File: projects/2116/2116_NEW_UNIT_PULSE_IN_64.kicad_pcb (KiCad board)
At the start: 2 copper layers, 166 x 180 mm, 172 parts, among them CN1 09031966921, CN10 HIF3FC-16PA-2.54DSA, CN11 HIF3FC-16PA-2.54DSA, CN2 09232486824, CN3 B2B-XH-A, CN4 HIF3FC-16PA-2.54DS, CN5 HIF3FC-16PA-2.54DS, CN6 HIF3FC-16PA-2.54DSA, CN7 HIF3FC-16PA-2.54DSA, CN8 HIF3FC-16PA-2.54DS, CN9 HIF3FC-16PA-2.54DS, IC1 74HCT32, IC10 74HC244, IC11 74HC244, IC12 74HC244, IC13 74HC14, IC14 74HC14, IC15 74HC14, IC16 74HC14, IC17 74HC14, IC18 74HC14, IC19 74HC244, IC2 74HCT138, IC20 74HC244, IC21 74HC244, IC22 74HC244, IC23 74HCT32, IC24 74HCT574, IC25 74HCT574, IC26 74HCT574, IC27 74HCT574, IC28 74HCT541, IC29 74HCT541, IC3 74HC14, IC30 74HCT541, IC31 74HCT541, IC32 74HCT574, IC33 74HCT574, IC34 74HCT574, IC35 74HCT574, IC36 74HCT541, IC37 74HCT541, IC38 74HCT541, IC39 74HCT541, IC4 74HC14, IC5 74HC14, IC6 74HC14, IC7 74HC14, IC8 74HC14, IC9 74HC244

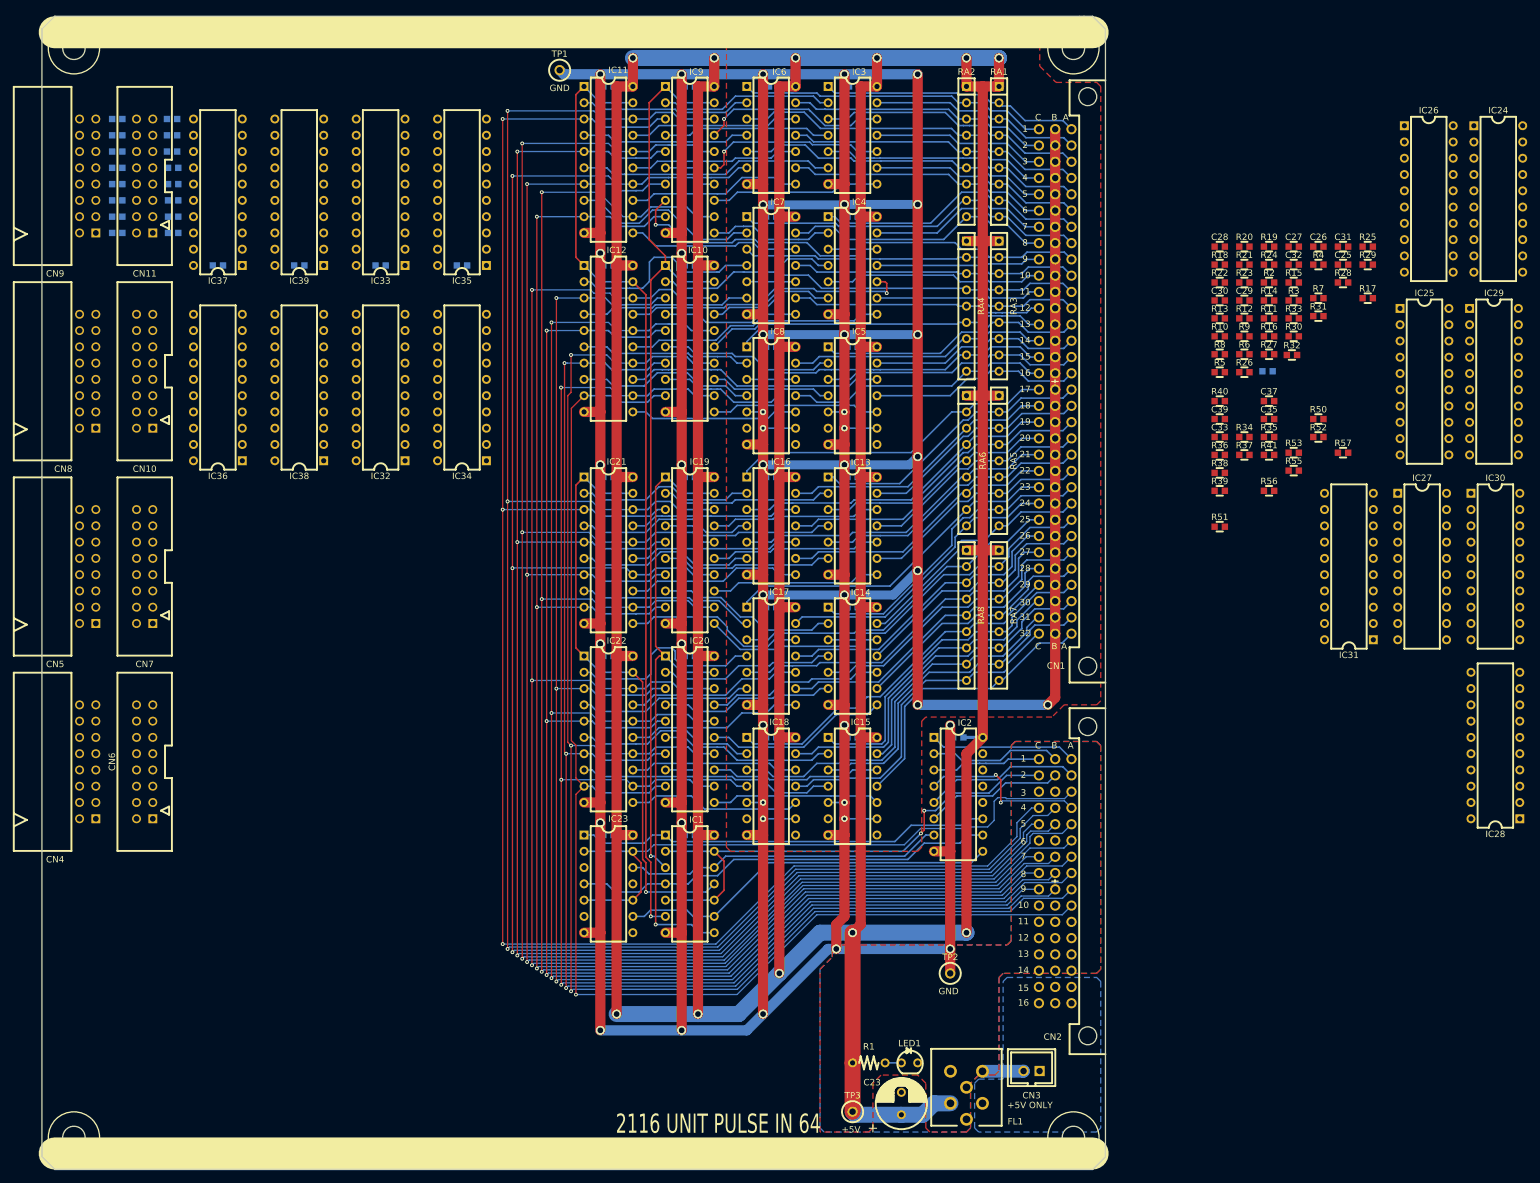
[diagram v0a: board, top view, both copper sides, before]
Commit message: 基板端に電源コネクタを追加。
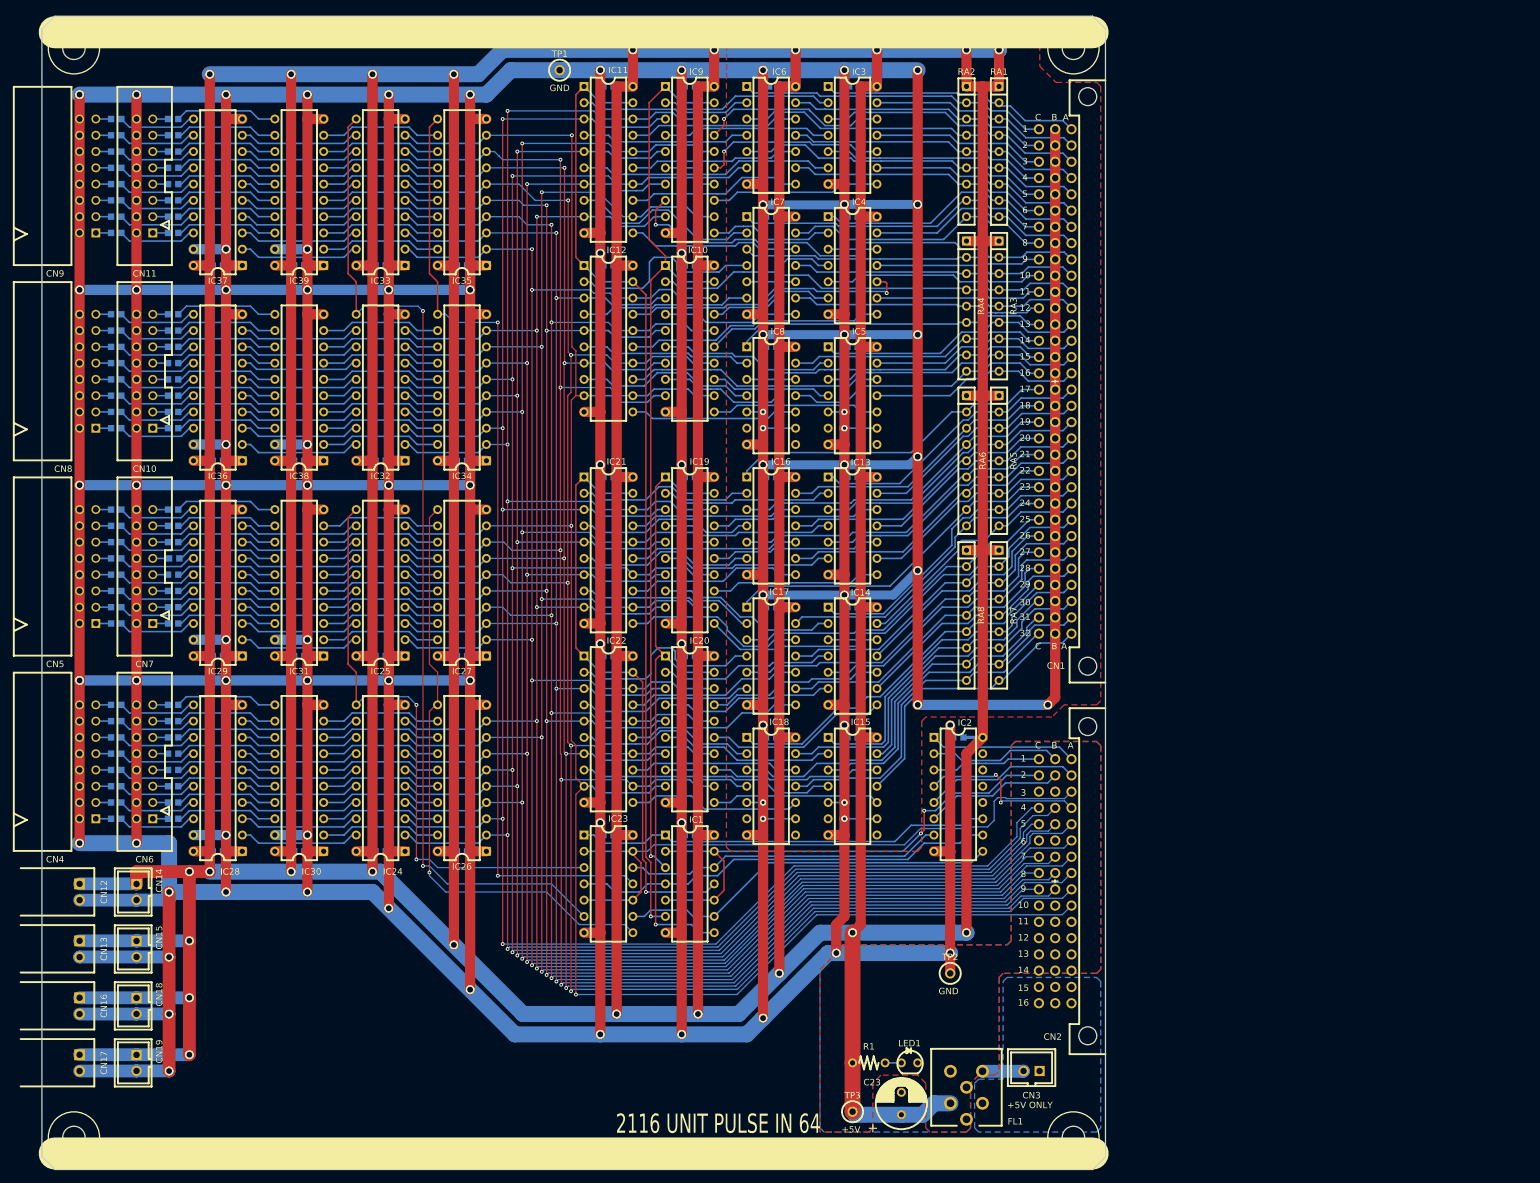
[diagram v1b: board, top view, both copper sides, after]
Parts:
- added CN12: S2B-XH-A, A01myFootPrint:S2B-XH-A, F.Cu at (55.9, 185.4)
- added CN13: S2B-XH-A, A01myFootPrint:S2B-XH-A, F.Cu at (55.9, 194.3)
- added CN14: B2B-XH-A, A01myFootPrint:cn_B2B-XH-A, F.Cu at (64.8, 186.7)
- added CN15: B2B-XH-A, A01myFootPrint:cn_B2B-XH-A, F.Cu at (64.8, 195.6)
- added CN16: S2B-XH-A, A01myFootPrint:S2B-XH-A, F.Cu at (55.9, 203.2)
- added CN17: S2B-XH-A, A01myFootPrint:S2B-XH-A, F.Cu at (55.9, 212.1)
- added CN18: B2B-XH-A, A01myFootPrint:cn_B2B-XH-A, F.Cu at (64.8, 204.5)
- added CN19: B2B-XH-A, A01myFootPrint:cn_B2B-XH-A, F.Cu at (64.8, 213.4)
- C25, C26, C27, C28, C29, C30, C31, C32, C33, C35, C37, C39, R10, R11, R12, R13, R14, R15, R16, R17, R18, R19, R2, R20, R21, R22, R23, R24, R25, R26, R27, R28, R29, R3, R30, R31, R32, R33, R34, R35, R36, R37, R38, R39, R4, R40, R41, R5, R50, R51, R52, R53, R55, R56, R57, R6, R7, R8, R9: moved to B.Cu
- moved R4 204.5 mm to (61.6, 170.2), turned to 180 degrees
- moved IC24 201.6 mm to (106.7, 180.3), turned to 180 degrees
- moved R3 199.8 mm to (61.6, 172.7), turned to 180 degrees
- moved R7 199.8 mm to (61.6, 162.6), turned to 180 degrees
- moved R25 199.7 mm to (70.5, 157.5), turned to 180 degrees
- moved IC28 199.5 mm to (81.3, 180.3)
- moved IC29 199.1 mm to (81.3, 149.9), turned to 180 degrees
- moved R2 198.5 mm to (61.6, 175.3), turned to 180 degrees
- moved R17 198.1 mm to (61.6, 127.0), turned to 180 degrees
- moved R29 192.6 mm to (70.5, 137.2), turned to 180 degrees
- moved R19 191.8 mm to (70.5, 172.7), turned to 180 degrees
- moved R28 188.8 mm to (70.5, 139.7), turned to 180 degrees
- moved C31 188.3 mm to (90.2, 180.3)
- moved R15 188.2 mm to (61.6, 132.1), turned to 180 degrees
- moved IC30 187.6 mm to (94.0, 180.3), turned to 180 degrees
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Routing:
- net GND: track 1188.5 -> 2561.7 mm, vias 43 -> 85
- net +5V: track 1026.3 -> 1875.7 mm, vias 11 -> 23
- net /W01: track 0.00 -> 157.8 mm, vias 0 -> 2
- net /W03: track 0.00 -> 149.4 mm, vias 0 -> 2
- net /D15: track 205.8 -> 301.6 mm, vias 1 -> 3
- net /W02: track 0.00 -> 94.1 mm, vias 0 -> 1
- net /W00: track 0.00 -> 92.8 mm, vias 0 -> 2
- net /D14: track 224.4 -> 311.8 mm, vias 3 -> 5
- net /D13: track 213.3 -> 295.5 mm, vias 3 -> 5
- net /D12: track 231.9 -> 310.7 mm, vias 3 -> 5
- net /D11: track 222.8 -> 289.0 mm, vias 3 -> 5
- net /D10: track 241.3 -> 305.4 mm, vias 3 -> 5
- net /D9: track 229.9 -> 289.1 mm, vias 3 -> 5
- net /D8: track 251.4 -> 299.6 mm, vias 3 -> 5
- net /D6: track 269.8 -> 314.6 mm, vias 3 -> 5
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
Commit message: ロン君の署名を追加。
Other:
- board text added: "Designed by Hamahara san Made by Long"
